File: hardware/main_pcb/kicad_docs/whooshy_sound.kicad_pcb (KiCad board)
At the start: 4 copper layers, 83.8 x 80 mm, 115 parts, among them J1 audio_in, J10 SWD_header, J2 audio_out, J3 extern_cutoff_CV_TRS, J4 extern_rez_CV_TRS, J5 9VDC_in, J6 signal_in, J7 signal_out, J8 cutoff_CV_in, J9 rez_CV_and_PS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

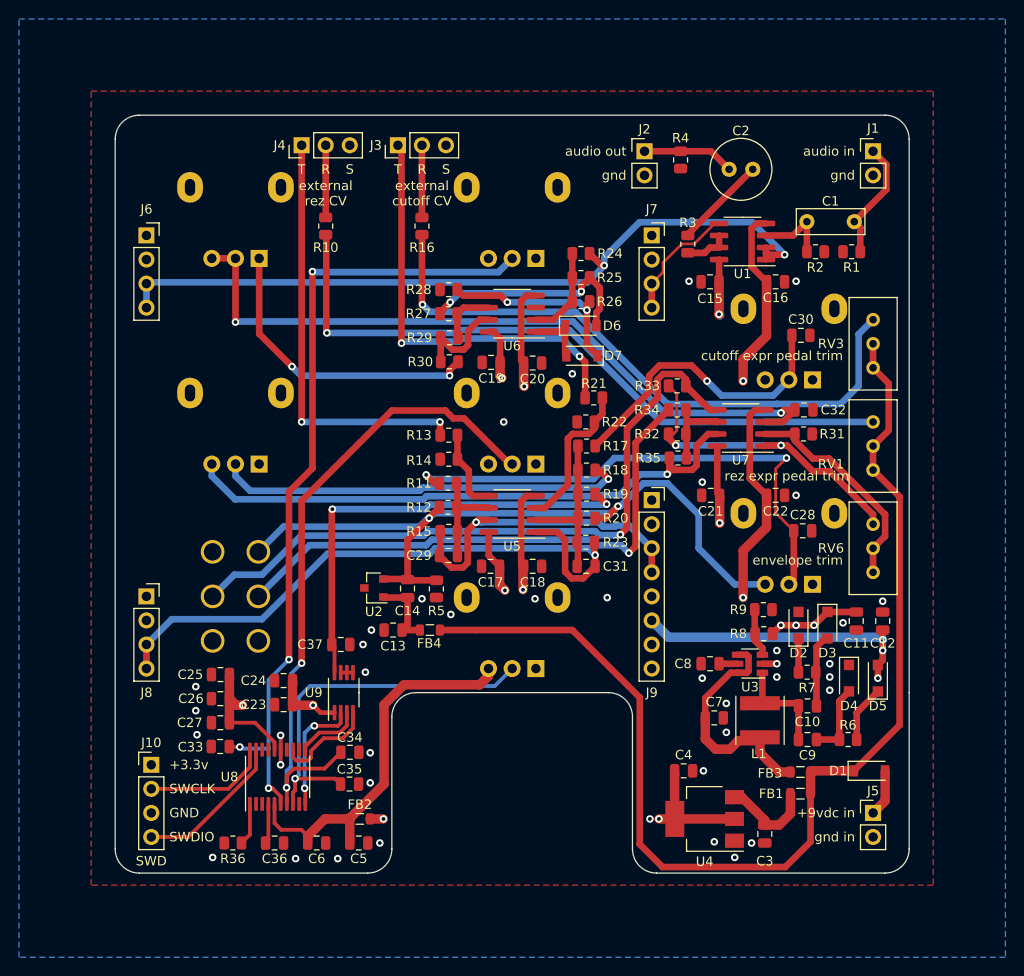
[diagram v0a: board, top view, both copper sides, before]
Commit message: move main pcb into its own dir
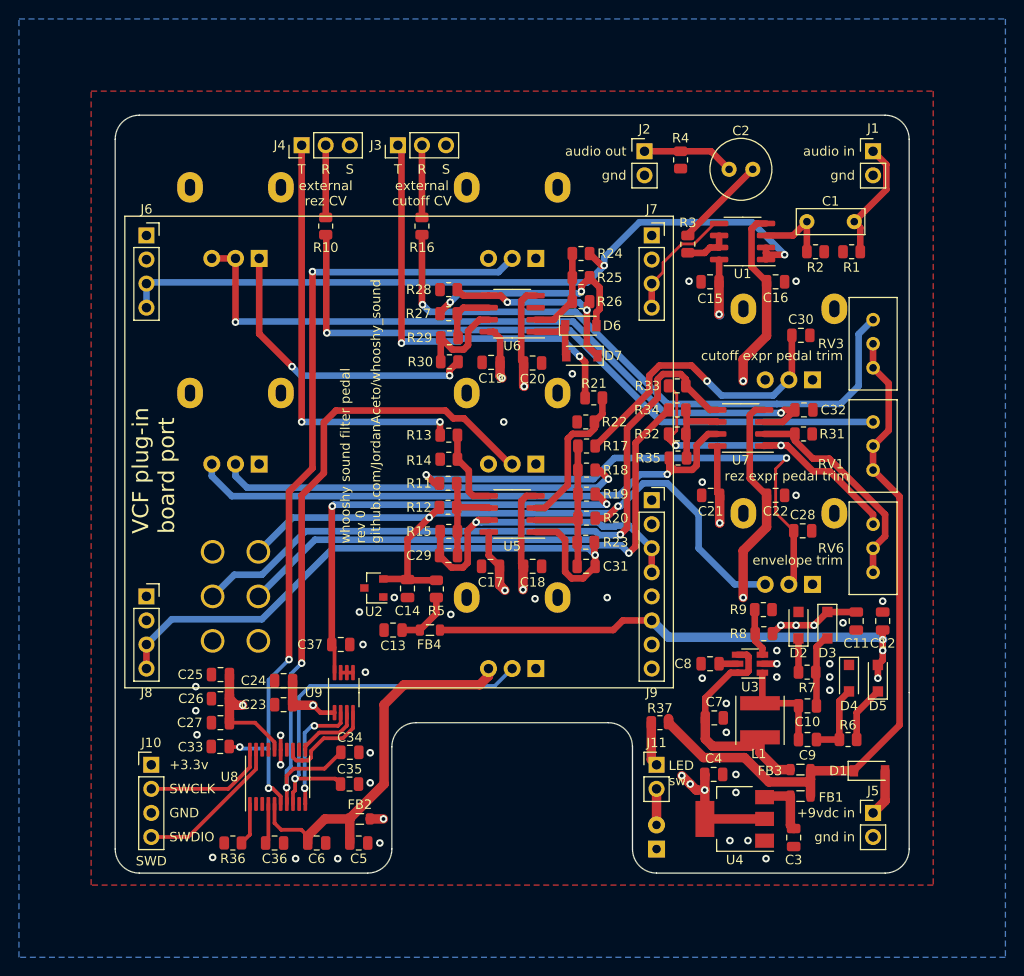
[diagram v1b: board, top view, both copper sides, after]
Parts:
- added D8: LED, LED_THT:LED_D3.0mm, B.Cu at (184.2, 148.6)
- added J11: LED_switch, Connector_PinHeader_2.54mm:PinHeader_1x02_P2.54mm_Vertical, F.Cu at (184.2, 139.7)
- added R37: 2k2, Resistor_SMD:R_0805_2012Metric, F.Cu at (184.5, 135.3)
- R5: value R -> 2k2
- moved C4 3.20 mm to (190.2, 140.7)
- moved U4 3.18 mm to (192.4, 145.4)
- moved C3 3.07 mm to (198.6, 147.4)
- moved FB1 0.25 mm to (199.3, 143.0)
- moved FB3 0.25 mm to (199.3, 140.2)
- turned C13 to 0 degrees
- turned FB4 to 180 degrees
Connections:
- C13 pad 1: Net-(C13-Pad1) -> GND
- C13 pad 2: GND -> Net-(C13-Pad2)
- C14 pad 1: Net-(C13-Pad1) -> GND
- FB4 pad 1: Net-(C13-Pad1) -> -12V
- FB4 pad 2: +9V -> Net-(C13-Pad2)
- R5 pad 2: GND -> Net-(C13-Pad2)
- U2 pad 1: Net-(C13-Pad1) -> GND
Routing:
- net +9V: track 121.3 -> 75.0 mm
- net -12V: track 185.6 -> 208.3 mm
- net Net-(C13-Pad1): track 8.13 -> 0.00 mm
- net Net-(C13-Pad2): track 0.00 -> 6.22 mm
- net Net-(J11-Pad1): track 0.00 -> 4.67 mm
- net Net-(D8-Pad2): track 0.00 -> 3.81 mm
- net Net-(C3-Pad1): track 10.0 -> 6.35 mm
- net /cutoff_CV_generator/LFO/shape_CV: track 69.2 -> 72.7 mm
- net +3V3: track 116.3 -> 117.4 mm, vias 5 -> 6
- net GND: track 6.38 -> 6.47 mm, vias 39 -> 40
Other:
- outline, holes or cut-outs redrawn
- board text added: "LED sw"
- board text added: "VCF plug-in board port"
- board text added: "whooshy sound filter pedal rev 0 github.com/JordanAceto/whooshy_sound"

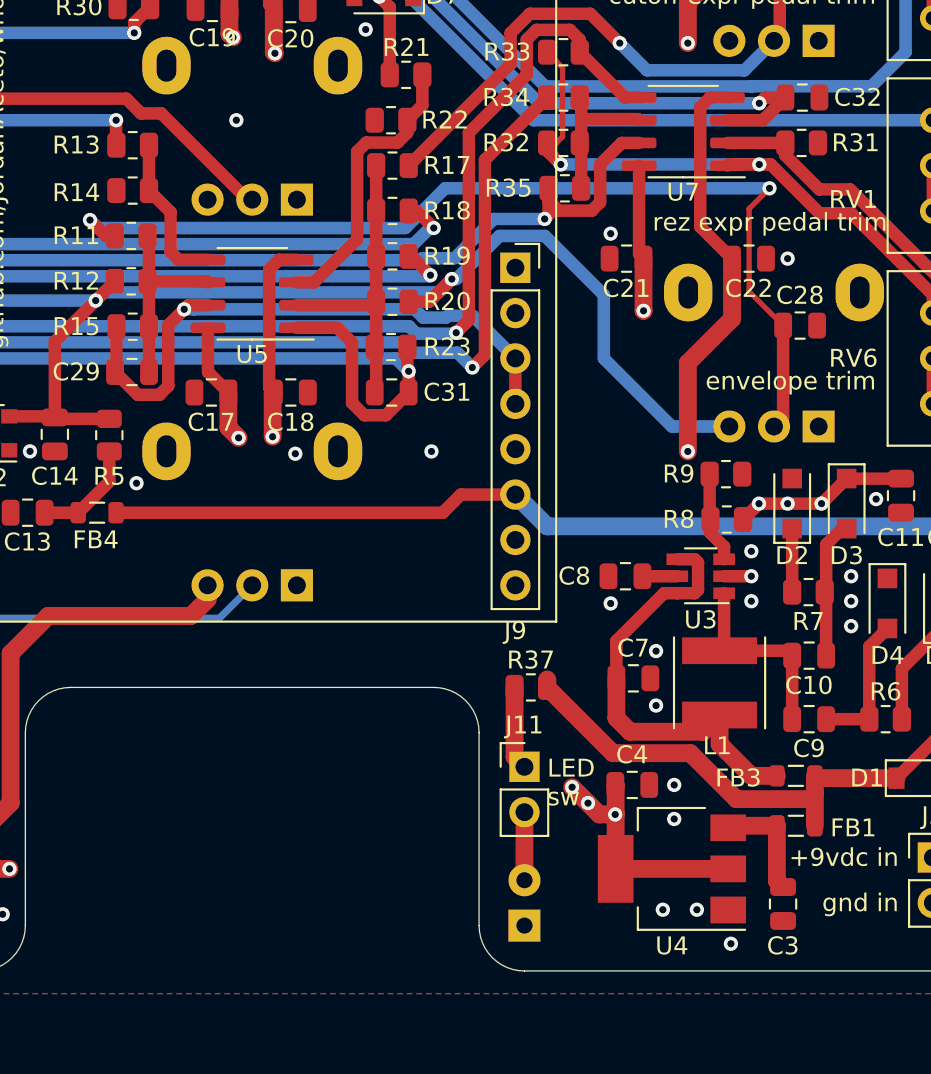
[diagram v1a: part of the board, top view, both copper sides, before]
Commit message: add LED driver, change LED to 5mm
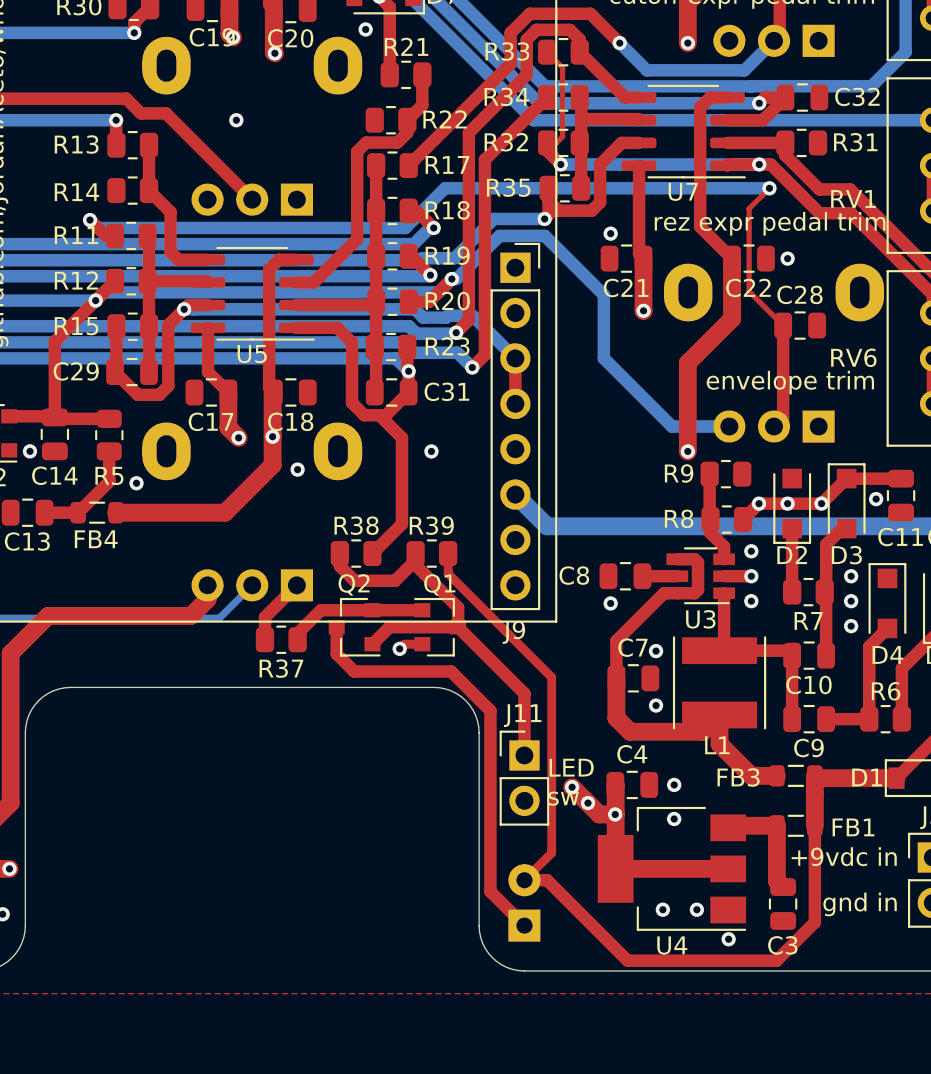
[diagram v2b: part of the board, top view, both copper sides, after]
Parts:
- added Q1: MMBT3904, Package_TO_SOT_SMD:SOT-23, F.Cu at (179.4, 131.9)
- added Q2: MMBT3904, Package_TO_SOT_SMD:SOT-23, F.Cu at (174.6, 131.9)
- added R38: 100k, Resistor_SMD:R_0805_2012Metric, F.Cu at (174.7, 127.8)
- added R39: 1M, Resistor_SMD:R_0805_2012Metric, F.Cu at (179.0, 127.8)
- D8: footprint LED_THT:LED_D3.0mm -> LED_THT:LED_D5.0mm
- R37: value 2k2 -> 100R
- moved R37 14.2 mm to (170.5, 132.6)
- moved J11 0.63 mm to (184.2, 139.1)
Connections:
- D8 pad 1: GND -> Net-(D8-Pad1)
- D8 pad 2: Net-(D8-Pad2) -> +9V
- J11 pad 2: Net-(D8-Pad2) -> GND
- R37 pad 1: +9V -> Net-(Q1-Pad1)
- R37 pad 2: Net-(J11-Pad1) -> GND
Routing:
- net +9V: track 75.0 -> 102.6 mm
- net Net-(D8-Pad1): track 0.00 -> 24.2 mm
- net Net-(J11-Pad1): track 4.67 -> 25.1 mm
- net -12V: track 208.3 -> 197.0 mm
- net /cutoff_CV_generator/summed_cutoff_CV_out: track 67.8 -> 76.8 mm
- net Net-(Q1-Pad1): track 0.00 -> 8.13 mm
- net GND: track 6.47 -> 11.9 mm, vias 40 -> 41
- net Net-(D8-Pad2): track 3.81 -> 0.00 mm
